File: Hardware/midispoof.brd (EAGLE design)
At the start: 76.2 x 47 mm, 21 parts, among them IC1 7805L, J1 DCJ0202, J2 STEREOSWS, M1 ARDUINO-NANO-3.0#ISP, U1 MICROCHIP_MCP41010-I-PMICROCH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

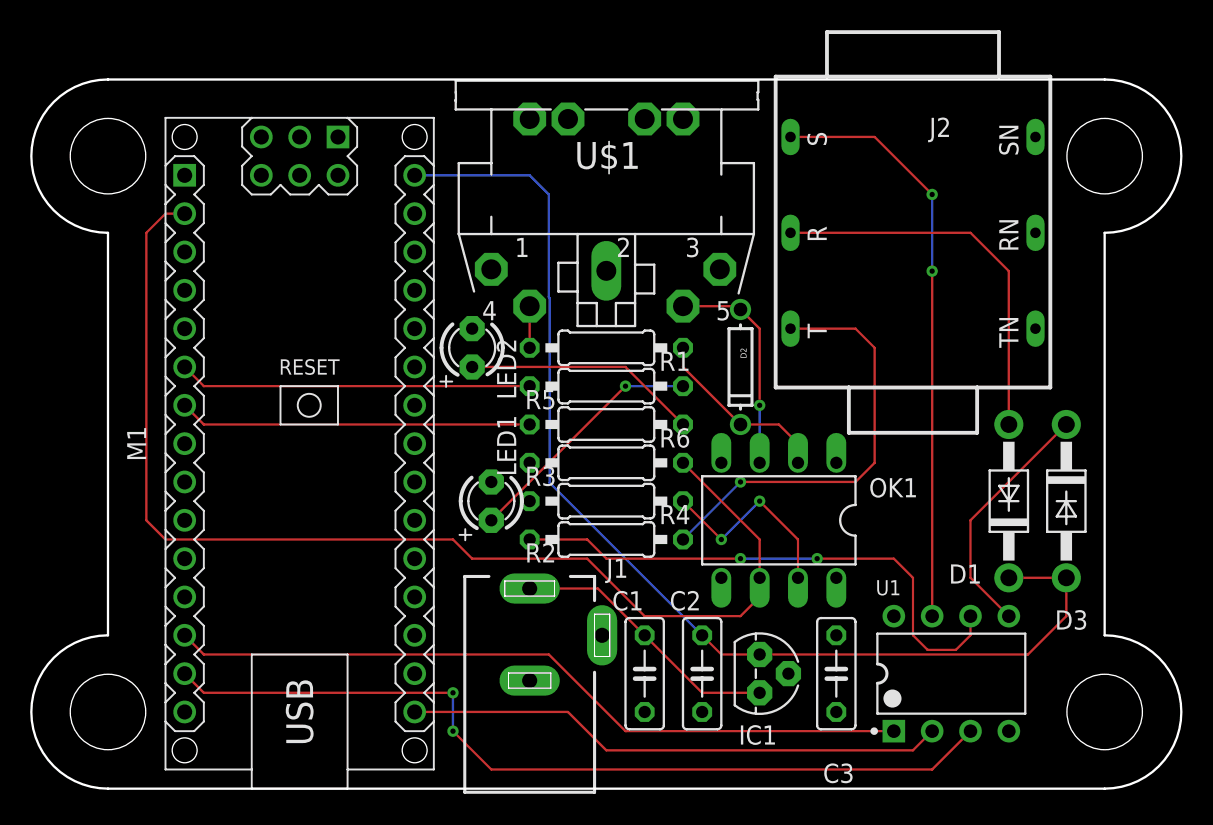
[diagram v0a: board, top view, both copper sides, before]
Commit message: Corrected missing supply flood fills on PCB layout
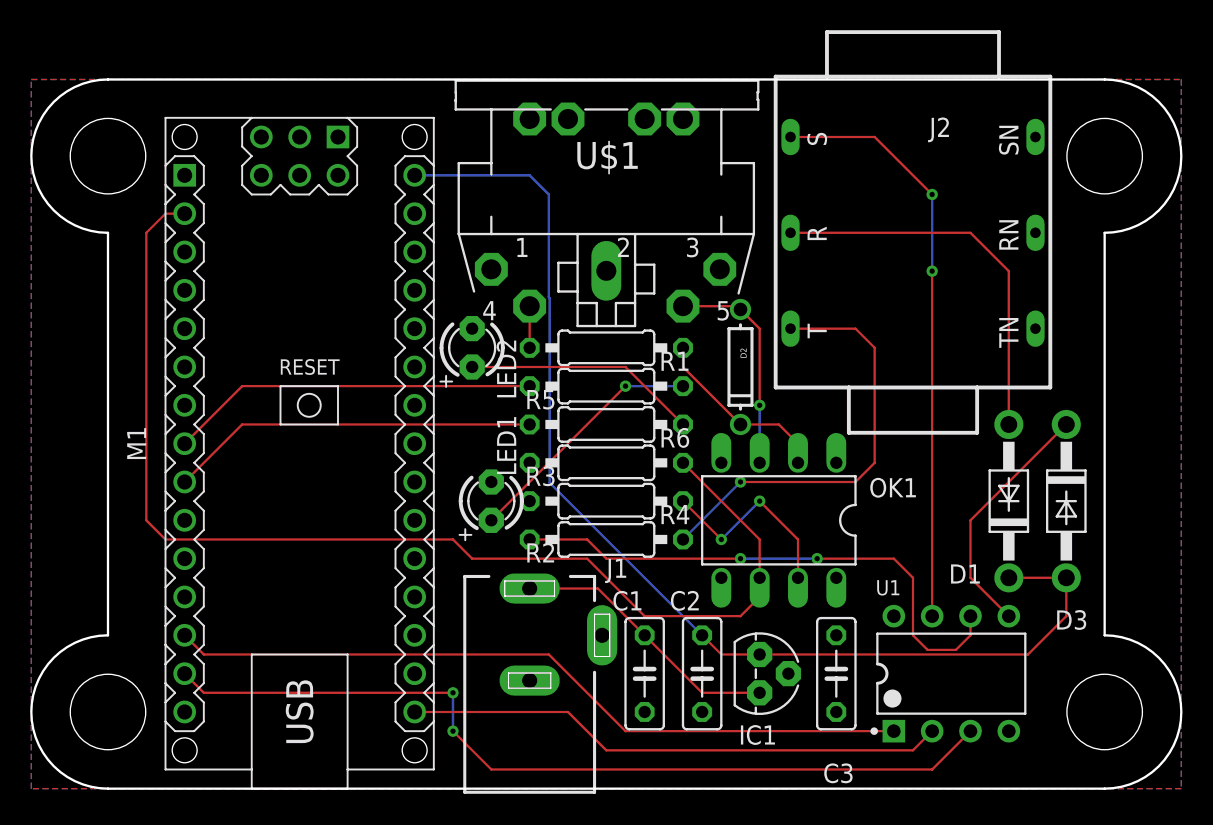
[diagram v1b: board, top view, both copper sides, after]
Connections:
- net N$18: now also M1.J1.8; no longer M1.J1.6
- net N$19: now also M1.J1.9; no longer M1.J1.7
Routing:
- net N$18: track 23.4 -> 24.4 mm
- net N$19: track 23.4 -> 24.4 mm
- added copper zone on layer 1, net +5V
- added copper zone on layer 16, net GND
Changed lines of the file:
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@@
 <drawing>
 <settings>
-<setting alwaysvectorfont="yes"/>
+<setting alwaysvectorfont="no"/>
 <setting verticaltext="up"/>
 </settings>
@@
 <contactref element="LED2" pad="K"/>
 <contactref element="LED1" pad="K"/>
-<wire x1="57.15" y1="20.32" x2="44.45" y2="25.4" width="0" layer="19" extent="1-1"/>
-<wire x1="49.25" y1="16.51" x2="57.15" y2="20.32" width="0" layer="19" extent="1-1"/>
-<wire x1="44.45" y1="13.51" x2="49.25" y2="16.51" width="0" layer="19" extent="1-1"/>
-<wire x1="52.07" y1="11.43" x2="49.25" y2="16.51" width="0" layer="19" extent="1-1"/>
-<wire x1="55.88" y1="11.43" x2="52.07" y2="11.43" width="0" layer="19" extent="1-1"/>
-<wire x1="61.595" y1="13.97" x2="55.88" y2="11.43" width="0" layer="19" extent="1-1"/>
-<wire x1="64.77" y1="11.43" x2="61.595" y2="13.97" width="0" layer="19" extent="1-1"/>
-<wire x1="76.2" y1="10.16" x2="64.77" y2="11.43" width="0" layer="19" extent="1-1"/>
-<wire x1="36.83" y1="44.45" x2="57.15" y2="20.32" width="0" layer="19" extent="1-1"/>
-<wire x1="21.59" y1="39.37" x2="36.83" y2="44.45" width="0" layer="19" extent="1-1"/>
-<wire x1="41.91" y1="26.67" x2="44.45" y2="13.51" width="0" layer="19" extent="1-1"/>
-<wire x1="40.64" y1="36.83" x2="41.91" y2="26.67" width="0" layer="19" extent="1-1"/>
+<polygon width="0.1524" layer="16">
+<vertex x="11.43" y="53.34"/>
+<vertex x="87.63" y="53.34"/>
+<vertex x="87.63" y="6.35"/>
+<vertex x="11.43" y="6.35"/>
+</polygon>
 </signal>
 <signal name="+5V" airwireshidden="yes">
@@
 <contactref element="OK1" pad="8"/>
 <contactref element="R3" pad="2"/>
-<wire x1="64.77" y1="16.51" x2="68.58" y2="17.78" width="0" layer="19" extent="1-1"/>
-<wire x1="64.77" y1="20.32" x2="64.77" y2="16.51" width="0" layer="19" extent="1-1"/>
-<wire x1="44.45" y1="27.94" x2="64.77" y2="20.32" width="0" layer="19" extent="1-1"/>
-<wire x1="36.83" y1="39.37" x2="64.77" y2="20.32" width="0" layer="19" extent="1-1"/>
+<polygon width="0.1524" layer="1">
+<vertex x="11.43" y="53.34"/>
+<vertex x="87.63" y="53.34"/>
+<vertex x="87.63" y="6.35"/>
+<vertex x="11.43" y="6.35"/>
+</polygon>
 </signal>
 <signal name="N$2">
@@
 </signal>
 <signal name="N$18">
-<contactref element="M1" pad="J1.6"/>
 <contactref element="R5" pad="2"/>
-<wire x1="44.45" y1="33.02" x2="22.86" y2="33.02" width="0.1524" layer="1"/>
-<wire x1="22.86" y1="33.02" x2="21.59" y2="34.29" width="0.1524" layer="1"/>
+<wire x1="44.45" y1="33.02" x2="25.4" y2="33.02" width="0.1524" layer="1"/>
+<contactref element="M1" pad="J1.8"/>
+<wire x1="25.4" y1="33.02" x2="21.59" y2="29.21" width="0.1524" layer="1"/>
 </signal>
 <signal name="N$19">
-<contactref element="M1" pad="J1.7"/>
 <contactref element="R6" pad="2"/>
-<wire x1="22.86" y1="30.48" x2="21.59" y2="31.75" width="0.1524" layer="1"/>
-<wire x1="44.45" y1="30.48" x2="22.86" y2="30.48" width="0.1524" layer="1"/>
+<contactref element="M1" pad="J1.9"/>
+<wire x1="25.4" y1="30.48" x2="21.59" y2="26.67" width="0.1524" layer="1"/>
+<wire x1="44.45" y1="30.48" x2="25.4" y2="30.48" width="0.1524" layer="1"/>
 </signal>
 </signals>
